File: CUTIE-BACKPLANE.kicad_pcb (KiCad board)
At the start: 4 copper layers, 57.5 x 86 mm, 15 parts, among them J1 ERF8-025-05.0-L-DV-L-K-TR, J2 ERF8-025-05.0-L-DV-L-K-TR, J3 ERF8-025-05.0-L-DV-L-K-TR, J4 ERF8-025-05.0-L-DV-L-K-TR, J7 USB3_A

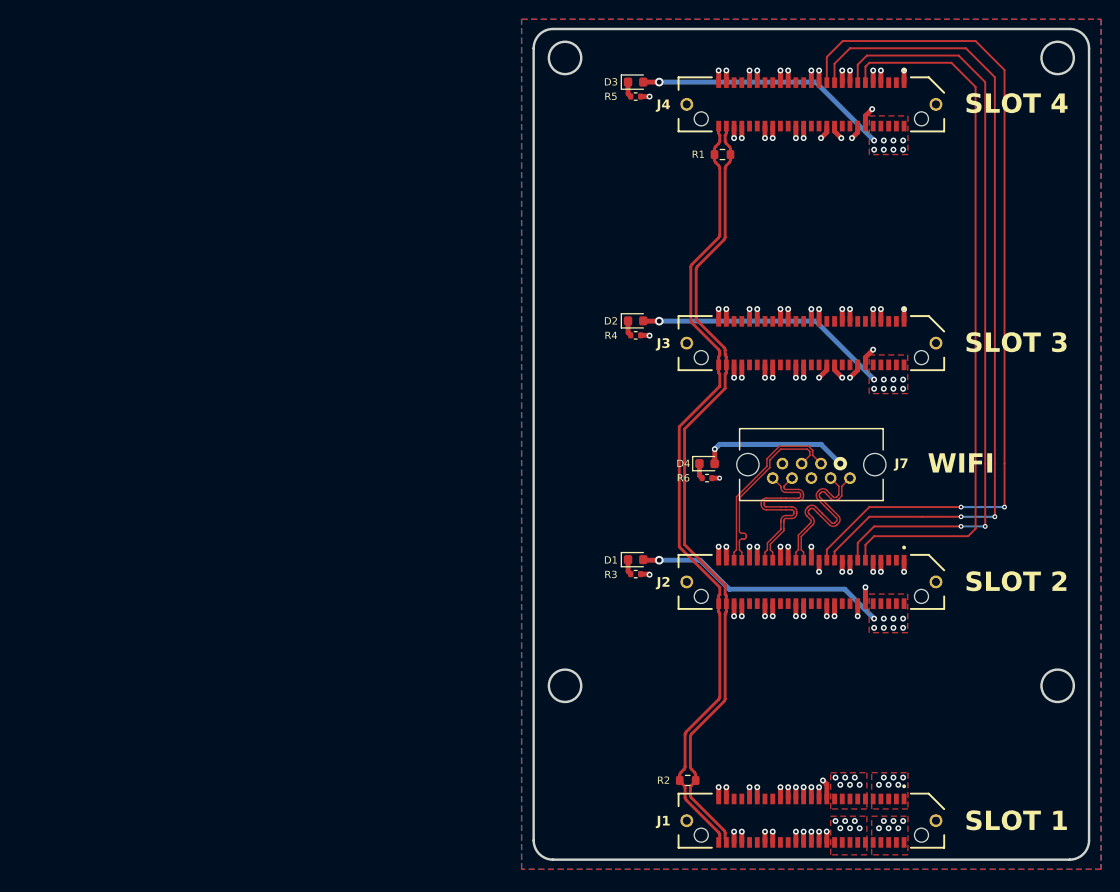
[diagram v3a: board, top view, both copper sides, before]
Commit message: silkscreen edits
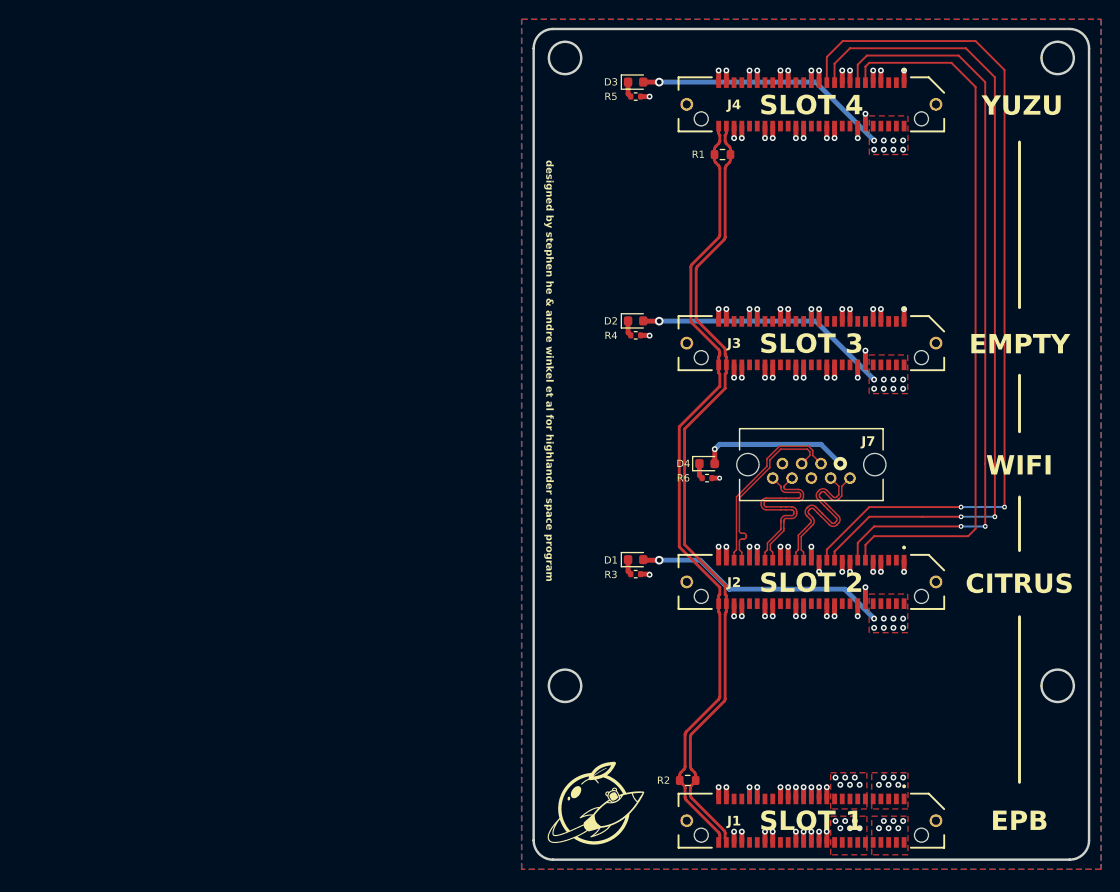
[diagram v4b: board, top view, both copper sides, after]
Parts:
- added G***: LOGO, LOGO, F.Cu at (130.7, 129.2)
- added G***: LOGO, LOGO, B.Cu at (151.3, 115.3)
- added G***: LOGO, LOGO, B.Cu at (153.1, 70.5)
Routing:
- net GND: track 120.1 -> 116.2 mm
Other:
- board text added: "CITRUS"
- board text added: "EMPTY"
- board text added: "EPB"
- board text added: "YUZU"
- board text added: "designed by stephen he & andre winkel et al for highlander space program"

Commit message: added dnps for can filtering
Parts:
- added C1: DNP, Capacitor_SMD:C_0402_1005Metric, F.Cu at (142.8, 64.2)
- added C2: DNP, Capacitor_SMD:C_0402_1005Metric, F.Cu at (144.8, 64.2)
- added C3: DNP, Capacitor_SMD:C_0402_1005Metric, F.Cu at (141.2, 124.6)
- added C4: DNP, Capacitor_SMD:C_0402_1005Metric, F.Cu at (139.2, 124.6)
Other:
- board text added: "ZEST"
- board text removed: "YUZU"

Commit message: added tps and new init layout
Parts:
- removed D4: LED Red, LED_SMD:LED_0603_1608Metric
- removed G*** (x3): LOGO, LOGO
- removed J7: USB3_A, library:CONN9_08-0003_MOL
- removed R6: 1k, Resistor_SMD:R_0402_1005Metric
- added 5VBUS1: TestPoint, library:KEYSTONE_575-4, F.Cu at (105.7, 112.0)
- added 5VBUS2: TestPoint, library:KEYSTONE_575-4, F.Cu at (105.7, 80.0)
- added 5VBUS3: TestPoint, library:KEYSTONE_575-4, F.Cu at (88.2, 112.0)
- added GND1: TestPoint, library:KEYSTONE_575-4, F.Cu at (105.7, 121.0)
- added GND2: TestPoint, library:KEYSTONE_575-4, F.Cu at (105.7, 71.0)
- added GND3: TestPoint, library:KEYSTONE_575-4, F.Cu at (88.2, 121.0)
- J1: value ERF8-025-05.0-L-DV-L-K-TR -> USB3_A; footprint library:SAMTEC_ERF8-025-05.0-L-DV-L-K-TR -> library:CONN9_08-0003_MOL
- R3, R4, R5: value 1k -> 330
- moved J4 84.3 mm to (78.4, 96.0), turned to -90 degrees
- moved J1 82.4 mm to (88.6, 79.5), turned to 90 degrees
- moved R2 77.1 mm to (74.3, 86.8), turned to 90 degrees
- moved D3 70.0 mm to (96.2, 112.9)
- moved R5 70.0 mm to (96.2, 114.4)
- moved C2 66.2 mm to (82.2, 85.7), turned to -90 degrees
- moved C1 65.0 mm to (82.2, 87.8), turned to 90 degrees
- moved J3 58.6 mm to (96.2, 96.0), turned to -90 degrees
- moved D1 57.1 mm to (78.4, 112.9)
- moved R3 57.1 mm to (78.4, 114.4)
- moved C4 49.8 mm to (108.1, 85.7), turned to -90 degrees
- moved C3 49.5 mm to (108.1, 87.8), turned to 90 degrees
- moved R1 42.2 mm to (109.7, 86.8), turned to 90 degrees
- moved D2 41.0 mm to (94.8, 70.1), turned to 90 degrees
- moved J2 40.3 mm to (114.1, 96.0), turned to -90 degrees
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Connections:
- C1 pad 2: /Slot 1/CAN0.N -> /CITRUS/CAN0.P
- C2 pad 2: /Slot 1/CAN0.P -> /CITRUS/CAN0.N
- C3 pad 2: /Slot 1/CAN0.P -> /CITRUS/CAN0.P
- C4 pad 2: /Slot 1/CAN0.N -> /CITRUS/CAN0.N
- D1 pad 2: /Slot 1/5V0_1 -> /LEMON/5VBUS3
- D2 pad 2: /Slot 1/5V0_2 -> /LEMON/5VBUS2
- D3 pad 2: /Slot 1/5V0_3 -> /CITRUS/5V0
- J2 pad 02: /Slot 1/5V0_1 -> GND
- J2 pad 03: unconnected-(J2-Pad03) -> GND
- J2 pad 04: /Slot 1/5V0_1 -> GND
- J2 pad 05: unconnected-(J2-Pad05) -> GND
- J2 pad 06: /Slot 1/5V0_1 -> GND
- J2 pad 08: /Slot 1/5V0_1 -> GND
- J2 pad 10: /Slot 1/5V0_1 -> GND
- J2 pad 11: /Slot 2/CMRF.CS0n -> GND
- J2 pad 13: /Slot 2/CMRF.SCLK -> GND
- J2 pad 15: GND -> /LEMON/5VBUS3
- J2 pad 16: unconnected-(J2-Pad16) -> GND
- J2 pad 17: GND -> /LEMON/5VBUS3
- J2 pad 18: unconnected-(J2-Pad18) -> GND
- J2 pad 19: /Slot 2/CMRF.MISO -> /LEMON/5VBUS3
- J2 pad 21: /Slot 2/CMRF.MOSI -> /LEMON/5VBUS3
- J2 pad 24: unconnected-(J2-Pad24) -> GND
- J2 pad 26: unconnected-(J2-Pad26) -> GND
- J2 pad 27: /Slot 2/USB3.TX_P -> /LEMON/5VBUS2
- J2 pad 29: /Slot 2/USB3.TX_N -> /LEMON/5VBUS2
- J2 pad 31: GND -> /LEMON/5VBUS2
- J2 pad 32: unconnected-(J2-Pad32) -> GND
- J2 pad 33: GND -> /LEMON/5VBUS2
- J2 pad 34: unconnected-(J2-Pad34) -> GND
- J2 pad 35: /Slot 2/USB3.RX_P -> GND
- J2 pad 37: /Slot 2/USB3.RX_N -> GND
- J2 pad 39: GND -> /CITRUS/5V0
- J2 pad 40: unconnected-(J2-Pad40) -> GND
- J2 pad 41: GND -> /CITRUS/5V0
- J2 pad 42: unconnected-(J2-Pad42) -> GND
- J2 pad 43: /Slot 2/USB3.D_P -> /CITRUS/5V0
- J2 pad 45: /Slot 2/USB3.D_N -> /CITRUS/5V0
- J2 pad 48: /Slot 1/CAN0.P -> /CITRUS/CAN0.P
- J2 pad 50: /Slot 1/CAN0.N -> /CITRUS/CAN0.N
- J3 pad 02: /Slot 1/5V0_2 -> /CITRUS/5V0
- J3 pad 03: unconnected-(J3-Pad03) -> GND
- J3 pad 04: /Slot 1/5V0_2 -> /CITRUS/5V0
- J3 pad 05: unconnected-(J3-Pad05) -> GND
- J3 pad 06: /Slot 1/5V0_2 -> /CITRUS/5V0
- J3 pad 08: /Slot 1/5V0_2 -> /CITRUS/5V0
- J3 pad 10: /Slot 1/5V0_2 -> /CITRUS/5V0
- J3 pad 11: unconnected-(J3-Pad11) -> /CITRUS/CMRF.CS0n
- J3 pad 13: unconnected-(J3-Pad13) -> /CITRUS/CMRF.SCLK
- J3 pad 16: unconnected-(J3-Pad16) -> GND
- J3 pad 18: unconnected-(J3-Pad18) -> GND
- J3 pad 19: unconnected-(J3-Pad19) -> /CITRUS/CMRF.MISO
- J3 pad 21: unconnected-(J3-Pad21) -> /CITRUS/CMRF.MOSI
- J3 pad 24: unconnected-(J3-Pad24) -> GND
- J3 pad 26: unconnected-(J3-Pad26) -> GND
- J3 pad 27: unconnected-(J3-Pad27) -> /CITRUS/USB3.TX_P
- J3 pad 29: unconnected-(J3-Pad29) -> /CITRUS/USB3.TX_N
- J3 pad 32: unconnected-(J3-Pad32) -> GND
- J3 pad 34: unconnected-(J3-Pad34) -> GND
- J3 pad 35: unconnected-(J3-Pad35) -> /CITRUS/USB3.RX_P
- J3 pad 37: unconnected-(J3-Pad37) -> /CITRUS/USB3.RX_N
- J3 pad 40: unconnected-(J3-Pad40) -> GND
- J3 pad 42: unconnected-(J3-Pad42) -> GND
- J3 pad 43: unconnected-(J3-Pad43) -> /CITRUS/USB3.D_P
- J3 pad 45: unconnected-(J3-Pad45) -> /CITRUS/USB3.D_N
- J3 pad 48: /Slot 1/CAN0.P -> /CITRUS/CAN0.P
- J3 pad 50: /Slot 1/CAN0.N -> /CITRUS/CAN0.N
- J4 pad 02: /Slot 1/5V0_3 -> /LEMON/5VBUS3
- J4 pad 03: unconnected-(J4-Pad03) -> GND
- J4 pad 04: /Slot 1/5V0_3 -> /LEMON/5VBUS3
- J4 pad 05: unconnected-(J4-Pad05) -> GND
- J4 pad 06: /Slot 1/5V0_3 -> /LEMON/5VBUS3
- J4 pad 08: /Slot 1/5V0_3 -> /LEMON/5VBUS3
- J4 pad 10: /Slot 1/5V0_3 -> /LEMON/5VBUS3
- J4 pad 11: /Slot 2/CMRF.CS0n -> /CITRUS/CMRF.CS0n
- J4 pad 13: /Slot 2/CMRF.SCLK -> /CITRUS/CMRF.SCLK
- J4 pad 16: unconnected-(J4-Pad16) -> GND
- J4 pad 18: unconnected-(J4-Pad18) -> GND
- J4 pad 19: /Slot 2/CMRF.MISO -> /CITRUS/CMRF.MISO
- J4 pad 21: /Slot 2/CMRF.MOSI -> /CITRUS/CMRF.MOSI
- J4 pad 24: unconnected-(J4-Pad24) -> GND
- J4 pad 26: unconnected-(J4-Pad26) -> GND
- J4 pad 27: unconnected-(J4-Pad27) -> GND
- J4 pad 29: unconnected-(J4-Pad29) -> GND
- J4 pad 32: unconnected-(J4-Pad32) -> GND
- J4 pad 34: unconnected-(J4-Pad34) -> GND
- J4 pad 35: unconnected-(J4-Pad35) -> GND
- J4 pad 37: unconnected-(J4-Pad37) -> GND
- J4 pad 40: unconnected-(J4-Pad40) -> GND
- J4 pad 42: unconnected-(J4-Pad42) -> GND
- J4 pad 43: unconnected-(J4-Pad43) -> GND
- J4 pad 45: unconnected-(J4-Pad45) -> GND
- J4 pad 48: /Slot 1/CAN0.P -> /CITRUS/CAN0.P
- J4 pad 50: /Slot 1/CAN0.N -> /CITRUS/CAN0.N
- R1 pad 1: /Slot 1/CAN0.P -> /CITRUS/CAN0.P
- R1 pad 2: /Slot 1/CAN0.N -> /CITRUS/CAN0.N
- R2 pad 1: /Slot 1/CAN0.P -> /CITRUS/CAN0.P
- R2 pad 2: /Slot 1/CAN0.N -> /CITRUS/CAN0.N
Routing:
- net GND: track 116.2 -> 0.00 mm, vias 93 -> 0
- net /Slot 2/CMRF.MOSI: track 89.5 -> 0.00 mm, vias 2 -> 0
- net /Slot 2/CMRF.MISO: track 84.9 -> 0.00 mm, vias 2 -> 0
- net /Slot 1/CAN0.P: track 84.0 -> 0.00 mm
- net /Slot 1/CAN0.N: track 84.0 -> 0.00 mm
- net /Slot 2/CMRF.SCLK: track 78.3 -> 0.00 mm, vias 2 -> 0
- net /Slot 2/CMRF.CS0n: track 73.7 -> 0.00 mm
- net /Slot 1/5V0_1: track 26.4 -> 0.00 mm, vias 15 -> 0
- net /Slot 1/5V0_2: track 26.4 -> 0.00 mm, vias 15 -> 0
- net /Slot 1/5V0_3: track 26.4 -> 0.00 mm, vias 15 -> 0
- net /Slot 2/USB3.D_N: track 19.1 -> 0.00 mm
- net /Slot 2/USB3.D_P: track 19.1 -> 0.00 mm
- net /Slot 2/USB3.RX_P: track 19.0 -> 0.00 mm
- net /Slot 2/USB3.RX_N: track 19.0 -> 0.00 mm
- net /Slot 2/USB3.TX_P: track 19.0 -> 0.00 mm
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- removed copper zone on F.Cu, net /Slot 1/5V0_1
- removed copper zone on In2.Cu, net /Slot 1/5V0_1
- removed copper zone on F.Cu, net /Slot 1/5V0_2
- removed copper zone on In2.Cu, net /Slot 1/5V0_2
- removed copper zone on F.Cu, net /Slot 1/5V0_3
- removed copper zone on In2.Cu, net /Slot 1/5V0_3
- removed copper zone on F.Cu, net /Slot 1/5V0_USB
- removed copper zone on In2.Cu, net /Slot 1/5V0_USB
- removed copper zone on B.Cu, net GND
- removed copper zone on F.Cu, net GND
- removed copper zone on In1.Cu, net GND
- removed copper zone on In2.Cu, net GND
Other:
- board size 57.5 x 86 mm -> 50.5 x 59.9 mm
- board text removed: "CITRUS"
- board text removed: "EMPTY"
- board text removed: "EPB"
- board text removed: "SLOT 1"
- board text removed: "SLOT 2"
- board text removed: "SLOT 3"
- board text removed: "SLOT 4"
- board text removed: "WIFI"
- board text removed: "ZEST"
- board text removed: "designed by stephen he & andre winkel et al for highlander space program"

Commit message: layout complete pending review
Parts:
- removed GND1, GND2: TestPoint, library:KEYSTONE_575-4
- moved 5VBUS1 40.2 mm to (110.0, 72.0)
- moved D3 37.7 mm to (110.0, 77.8)
- moved R5 37.6 mm to (110.0, 79.4)
- moved C4 22.6 mm to (110.0, 108.2), turned to 90 degrees
- moved C2 20.6 mm to (83.8, 106.2), turned to 90 degrees
- moved R1 20.3 mm to (118.2, 105.2), turned to -90 degrees
- moved R2 20.1 mm to (82.4, 105.2), turned to -90 degrees
- moved C3 18.5 mm to (110.0, 106.2), turned to -90 degrees
- moved C1 16.5 mm to (83.8, 104.2), turned to -90 degrees
- moved GND3 16.3 mm to (104.5, 120.0)
- moved 5VBUS2 10.4 mm to (99.0, 72.0)
- moved R4 9.66 mm to (99.0, 79.4), turned to 0 degrees
- moved R3 8.81 mm to (87.0, 112.5), turned to 180 degrees
- moved D2 8.77 mm to (99.0, 77.8), turned to 0 degrees
- moved D1 8.67 mm to (87.0, 114.0), turned to 180 degrees
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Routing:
- net /CITRUS/CAN0.N: track 0.00 -> 42.0 mm
- net /CITRUS/CAN0.P: track 0.00 -> 42.0 mm
- net /CITRUS/USB3.D_N: track 0.00 -> 34.5 mm
- net /CITRUS/USB3.D_P: track 0.00 -> 34.4 mm
- net /CITRUS/USB3.TX_P: track 0.00 -> 34.4 mm
- net /CITRUS/USB3.TX_N: track 0.00 -> 34.4 mm
- net /CITRUS/USB3.RX_P: track 0.00 -> 34.3 mm
- net /CITRUS/USB3.RX_N: track 0.00 -> 34.3 mm
- net /CITRUS/CMRF.CS0n: track 0.00 -> 18.5 mm, vias 0 -> 2
- net /CITRUS/CMRF.SCLK: track 0.00 -> 18.5 mm, vias 0 -> 2
- net /CITRUS/CMRF.MOSI: track 0.00 -> 18.5 mm, vias 0 -> 2
- net /CITRUS/CMRF.MISO: track 0.00 -> 18.5 mm, vias 0 -> 2
- net /LEMON/5VBUS3: track 0.00 -> 6.33 mm, vias 0 -> 15
- net /LEMON/5VBUS2: track 0.00 -> 6.13 mm, vias 0 -> 6
- net /CITRUS/5V0: track 0.00 -> 6.13 mm
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- added copper zone on F.Cu, net /CITRUS/5V0
- added copper zone on F.Cu, net /LEMON/5VBUS2
- added copper zone on In2.Cu, net /LEMON/5VBUS2
- added copper zone on F.Cu, net /LEMON/5VBUS3
- added copper zone on In2.Cu, net /LEMON/5VBUS3
- added copper zone on B.Cu, net GND
- added copper zone on F.Cu, net GND
- added copper zone on In1.Cu, net GND
- added copper zone on In2.Cu, net GND

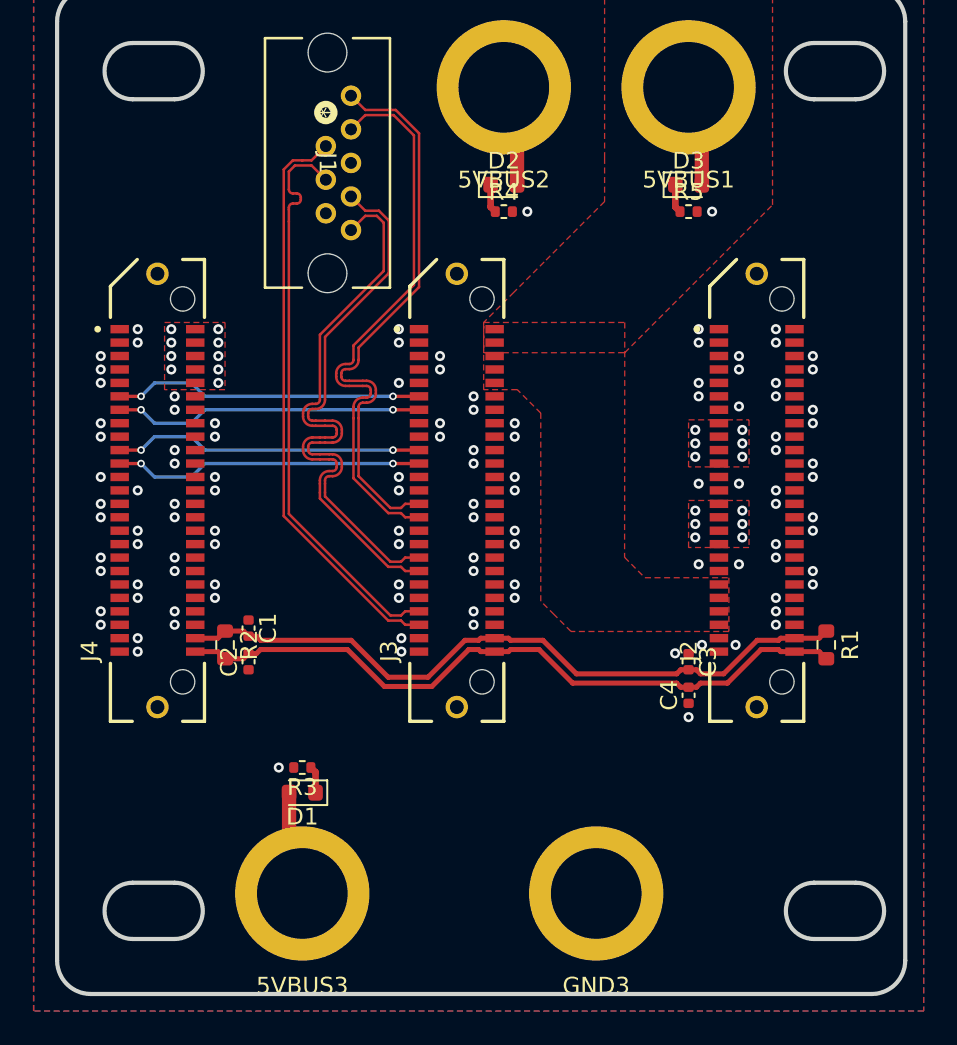
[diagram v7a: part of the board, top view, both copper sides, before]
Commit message: moved connectors, added silkscreen
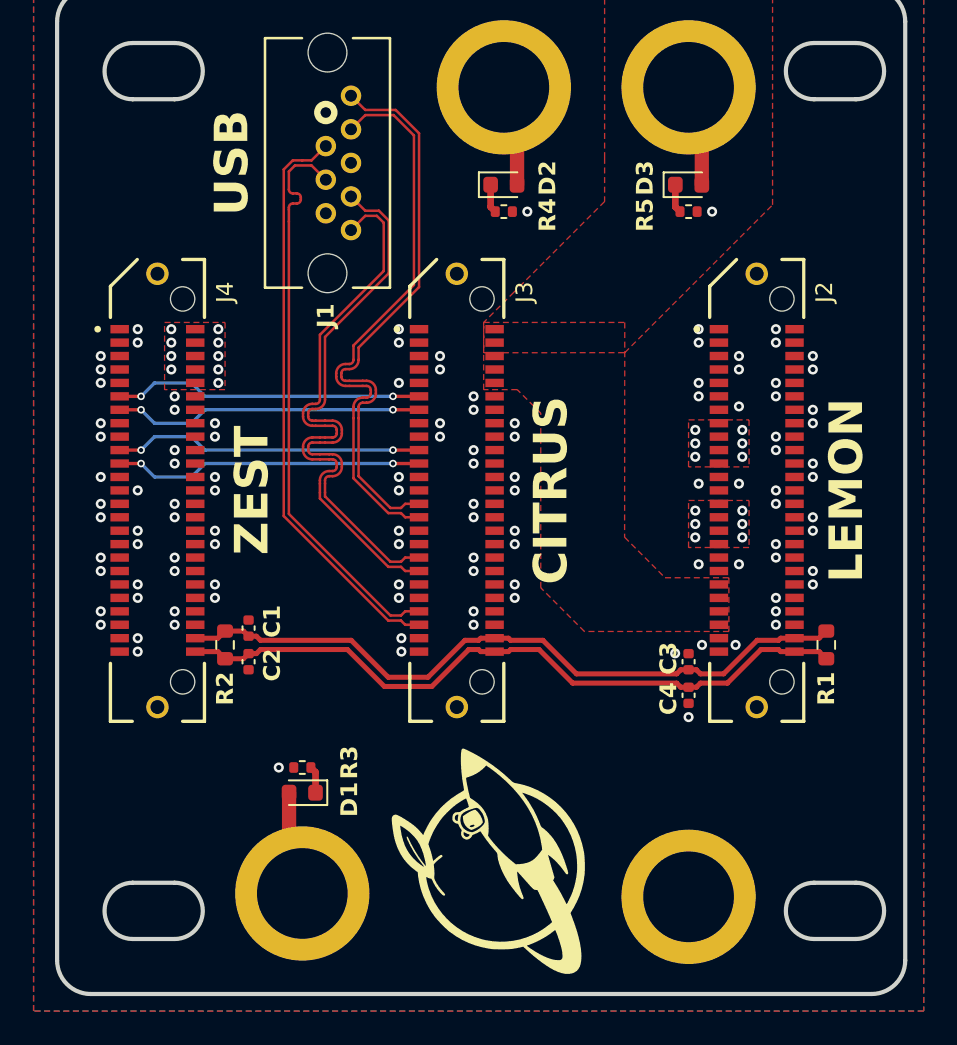
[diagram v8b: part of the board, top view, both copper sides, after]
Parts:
- removed GND3: TestPoint, library:KEYSTONE_575-4
- added G***: LOGO, LOGO, F.Cu at (98.1, 118.1)
- added G***: LOGO, LOGO, B.Cu at (102.9, 98.4)
- added GND: TestPoint, library:KEYSTONE_575-4, B.Cu at (110.0, 120.2)
- 5VBUS1, 5VBUS2, 5VBUS3: moved to B.Cu
- turned 5VBUS1 to 180 degrees
- turned 5VBUS2 to 180 degrees
- turned 5VBUS3 to 180 degrees
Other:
- board text added: "A"
- board text added: "Board"
- board text added: "CITRUS"
- board text added: "CUTIE-BACKPLANE"
- board text added: "LEMON"
- board text added: "Revision"
- board text added: "SN"
- board text added: "USB"
- board text added: "ZEST"
